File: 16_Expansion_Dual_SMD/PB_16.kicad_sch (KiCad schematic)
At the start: 27 parts, among them J17 Power In Left, J18 Power In Right, J19 Expansion Header, J20 v4 Input

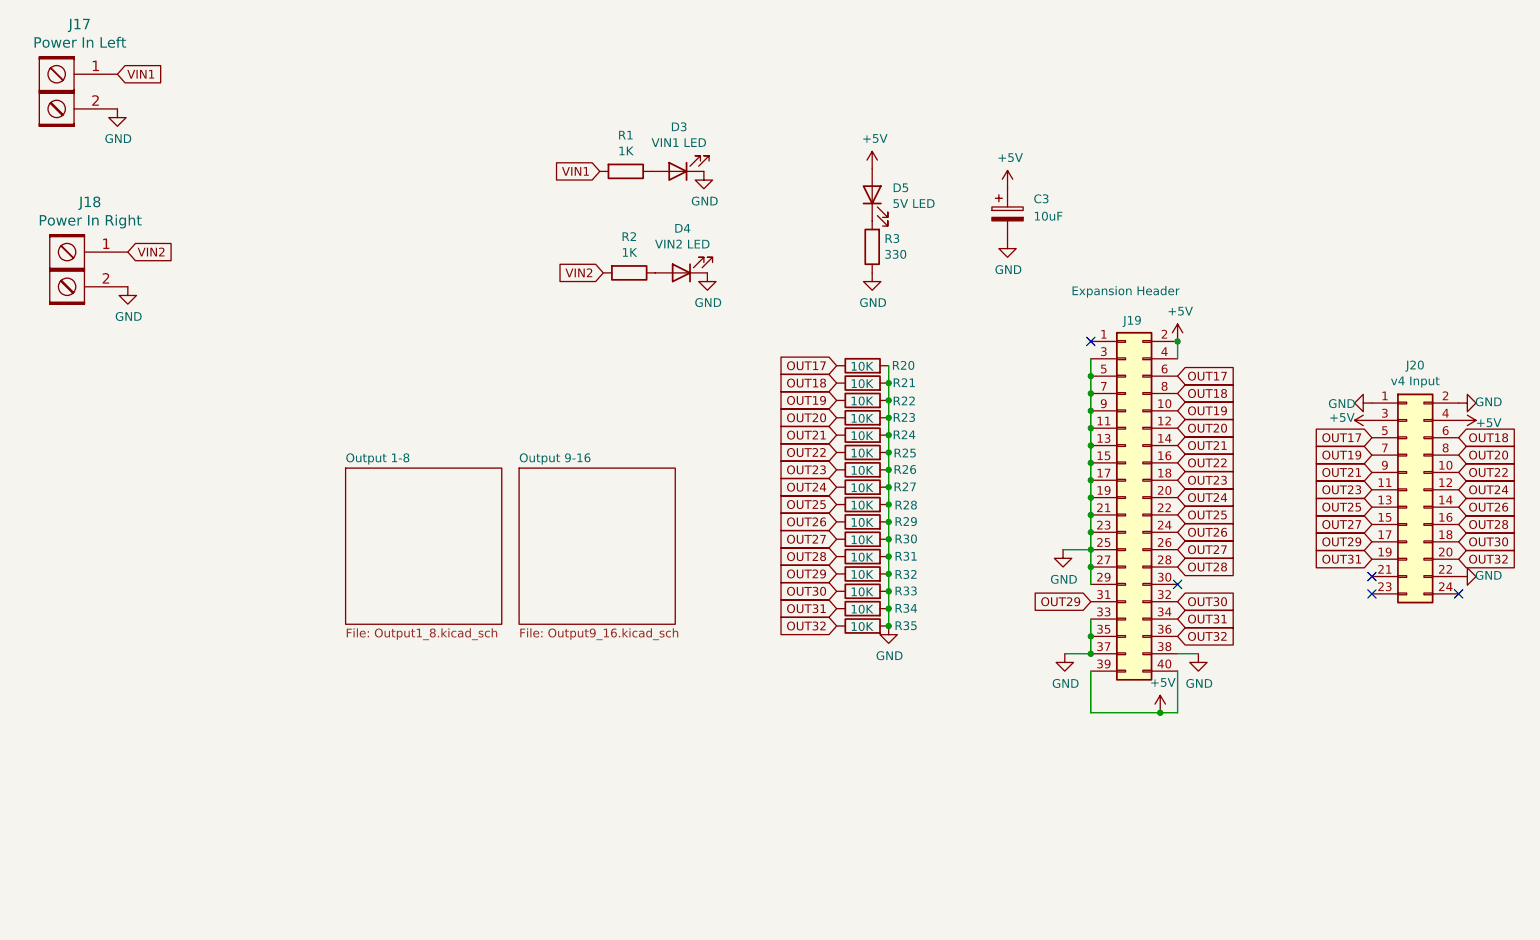
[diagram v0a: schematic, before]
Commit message: added 120 ohm filter resistors
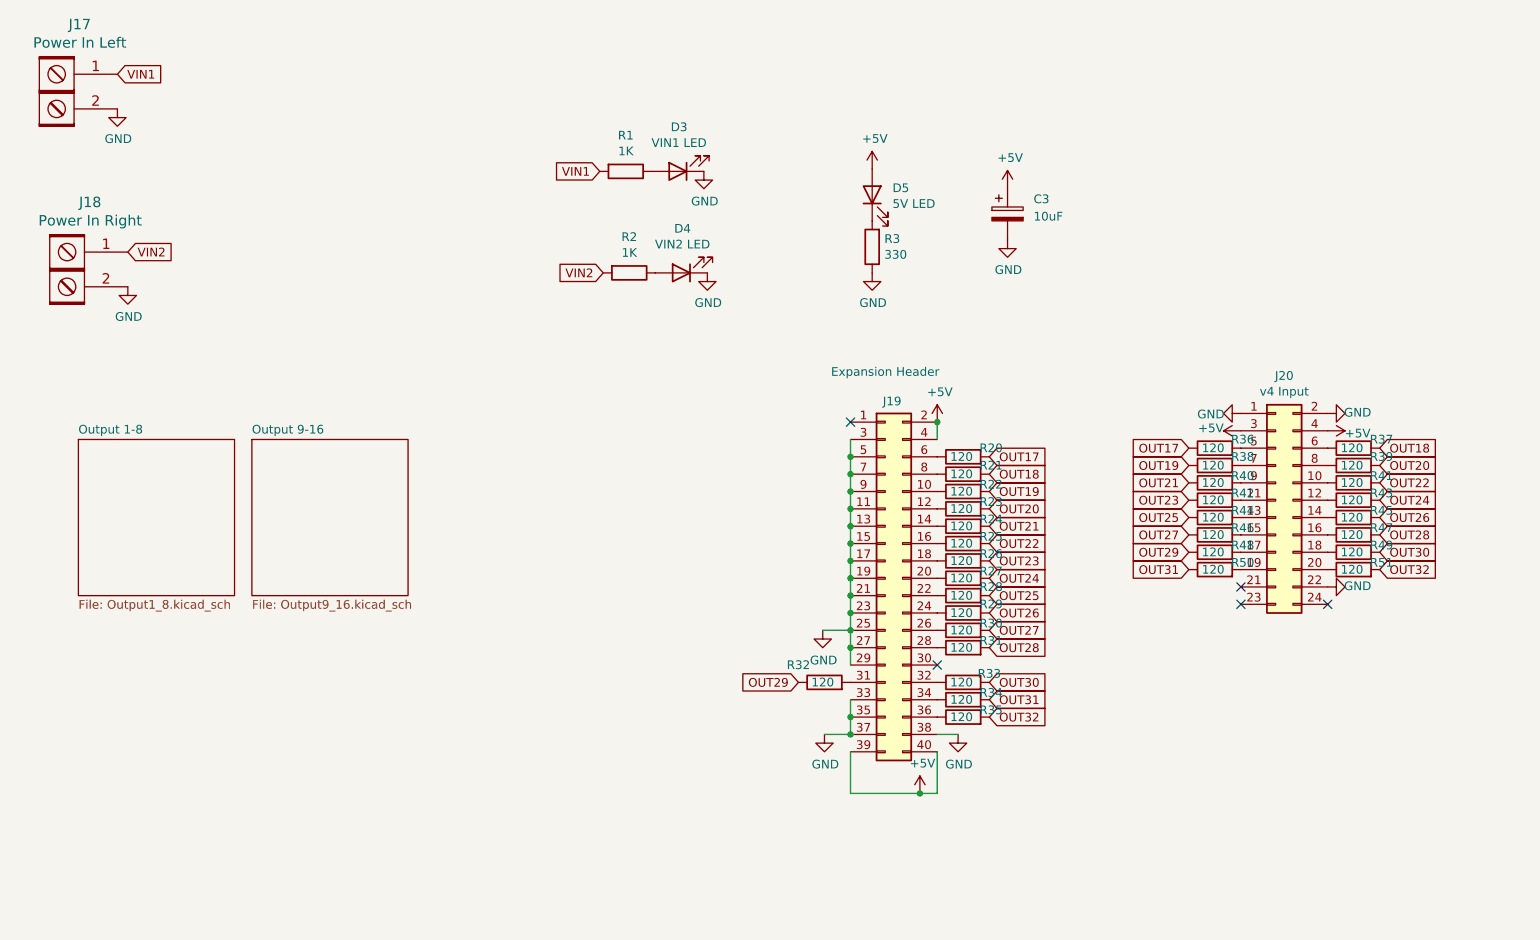
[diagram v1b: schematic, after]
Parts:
- added R36, R37, R38, R39, R40, R41, R42, R43, R44, R45, R46, R47, R48, R49, R50, R51: 120, Resistor_SMD:R_0603_1608Metric_Pad0.98x0.95mm_HandSolder, symbol Device:R
- R20, R21, R22, R23, R24, R25, R26, R27, R28, R29, R30, R31, R32, R33, R34, R35: value 10K -> 120; Digi-Key_PN 311-10.0KHRCT-ND -> RMCF0603JT120RCT-ND; LCSC C25804 -> C22787; MPN RC0603FR-0710KL -> RMCF0603JT120R
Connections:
- net GND: no longer R20.2, R21.2, R22.2, R23.2, R24.2, R25.2, R26.2, R27.2, R28.2, R29.2, R30.2, R31.2, R32.2, R33.2, R34.2, R35.2
- net OUT17: now also R20.2, R36.1; no longer J19.6 (Pin_6), J20.5 (Pin_5), R20.1
- net OUT18: now also R21.2, R37.2; no longer J19.8 (Pin_8), J20.6 (Pin_6), R21.1
- net OUT19: now also R22.2, R38.1; no longer J19.10 (Pin_10), J20.7 (Pin_7), R22.1
- net OUT20: now also R23.2, R39.2; no longer J19.12 (Pin_12), J20.8 (Pin_8), R23.1
- net OUT21: now also R24.2, R40.1; no longer J19.14 (Pin_14), J20.9 (Pin_9), R24.1
- net OUT22: now also R25.2, R41.2; no longer J19.16 (Pin_16), J20.10 (Pin_10), R25.1
- net OUT23: now also R26.2, R42.1; no longer J19.18 (Pin_18), J20.11 (Pin_11), R26.1
- net OUT24: now also R27.2, R43.2; no longer J19.20 (Pin_20), J20.12 (Pin_12), R27.1
- net OUT25: now also R28.2, R44.1; no longer J19.22 (Pin_22), J20.13 (Pin_13), R28.1
- net OUT26: now also R29.2, R45.2; no longer J19.24 (Pin_24), J20.14 (Pin_14), R29.1
- net OUT27: now also R30.2, R46.1; no longer J19.26 (Pin_26), J20.15 (Pin_15), R30.1
- net OUT28: now also R31.2, R47.2; no longer J19.28 (Pin_28), J20.16 (Pin_16), R31.1
- net OUT29: now also R48.1; no longer J19.31 (Pin_31), J20.17 (Pin_17)
- net OUT30: now also R33.2, R49.2; no longer J19.32 (Pin_32), J20.18 (Pin_18), R33.1
- net OUT31: now also R34.2, R50.1; no longer J19.34 (Pin_34), J20.19 (Pin_19), R34.1
- net OUT32: now also R35.2, R51.2; no longer J19.36 (Pin_36), J20.20 (Pin_20), R35.1
- new net: J19.10 (Pin_10), R22.1
- new net: J19.12 (Pin_12), R23.1
- new net: J19.14 (Pin_14), R24.1
- new net: J19.16 (Pin_16), R25.1
- new net: J19.18 (Pin_18), R26.1
- new net: J19.20 (Pin_20), R27.1
- new net: J19.22 (Pin_22), R28.1
- new net: J19.24 (Pin_24), R29.1
- new net: J19.26 (Pin_26), R30.1
- new net: J19.28 (Pin_28), R31.1
- new net: J19.31 (Pin_31), R32.2
- new net: J19.32 (Pin_32), R33.1
- new net: J19.34 (Pin_34), R34.1
- new net: J19.36 (Pin_36), R35.1
- new net: J19.6 (Pin_6), R20.1
- new net: J19.8 (Pin_8), R21.1
- new net: J20.17 (Pin_17), R48.2
- new net: J20.9 (Pin_9), R40.2
- new net: J20.10 (Pin_10), R41.1
- new net: J20.11 (Pin_11), R42.2
- new net: J20.12 (Pin_12), R43.1
- new net: J20.13 (Pin_13), R44.2
- new net: J20.14 (Pin_14), R45.1
- new net: J20.15 (Pin_15), R46.2
- new net: J20.16 (Pin_16), R47.1
- new net: J20.18 (Pin_18), R49.1
- new net: J20.19 (Pin_19), R50.2
- new net: J20.20 (Pin_20), R51.1
- new net: J20.5 (Pin_5), R36.2
- new net: J20.6 (Pin_6), R37.1
- new net: J20.7 (Pin_7), R38.2
- new net: J20.8 (Pin_8), R39.1
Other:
- moved on the sheet: J19, J20

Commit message: update to expansions, add pico button board
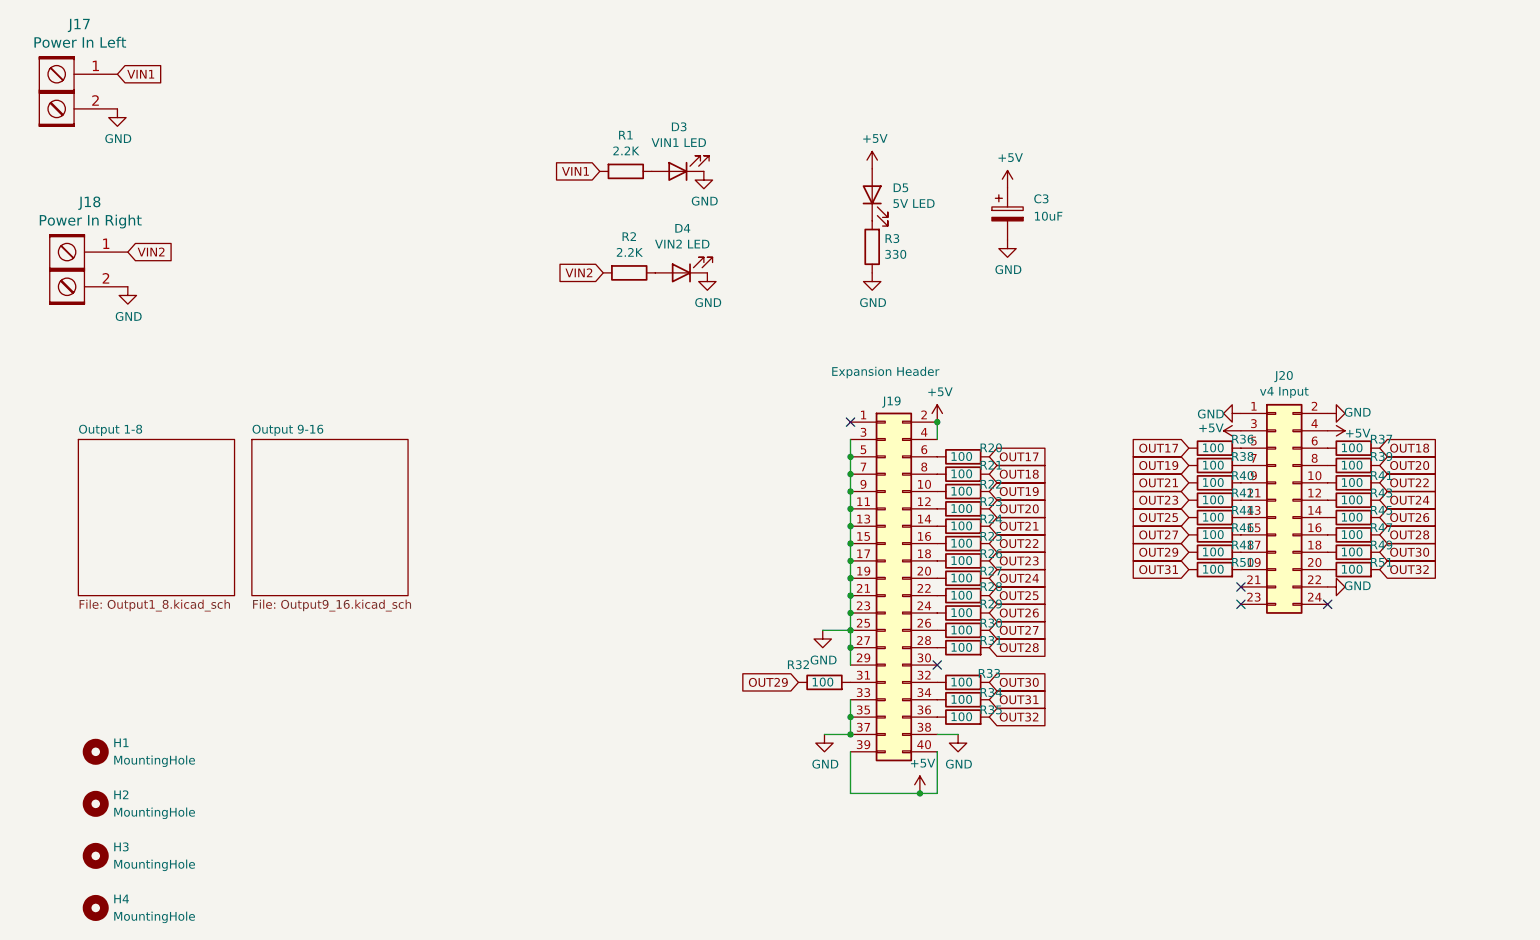
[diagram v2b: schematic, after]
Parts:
- added H1, H2, H3, H4: MountingHole, Scotts:MountingHole_3.7mm, symbol Mechanical:MountingHole
- D3, D4, D5: footprint LED_SMD:LED_0603_1608Metric_Pad1.05x0.95mm_HandSolder -> LED_SMD:LED_0603_1608Metric
- R1: value 1K -> 2.2K; footprint Resistor_SMD:R_0603_1608Metric_Pad0.98x0.95mm_HandSolder -> Resistor_SMD:R_0603_1608Metric; Digi-Key_PN 311-1.00KHRTR-ND -> (none); LCSC C21190 -> (none); MPN RC0603FR-071KL -> (none)
- R2: value 1K -> 2.2K; footprint Resistor_SMD:R_0603_1608Metric_Pad0.98x0.95mm_HandSolder -> Resistor_SMD:R_0603_1608Metric; LCSC C21190 -> (none)
- R20, R21, R22, R23, R24, R25, R26, R27, R28, R29, R30, R31, R32, R33, R34, R35, R36, R37, R38, R39, R40, R41, R42, R43, R44, R45, R46, R47, R48, R49, R50, R51: value 120 -> 100; footprint Resistor_SMD:R_0603_1608Metric_Pad0.98x0.95mm_HandSolder -> Resistor_SMD:R_0603_1608Metric; LCSC C22787 -> (none)
- R3: footprint Resistor_SMD:R_0603_1608Metric_Pad0.98x0.95mm_HandSolder -> Resistor_SMD:R_0603_1608Metric
